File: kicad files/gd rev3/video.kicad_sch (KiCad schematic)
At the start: 55 parts, among them J17 VGA_Micro, J18 vga_SWD, J22 L77HDE15SD1CH4F, SW6 VGA Boot Sel, SW7 VGA RESET, U19 W25Q128JVS, U22 74HCT245, U23 RP2040, U24 74LVC2G04, U25 74LVC2G04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

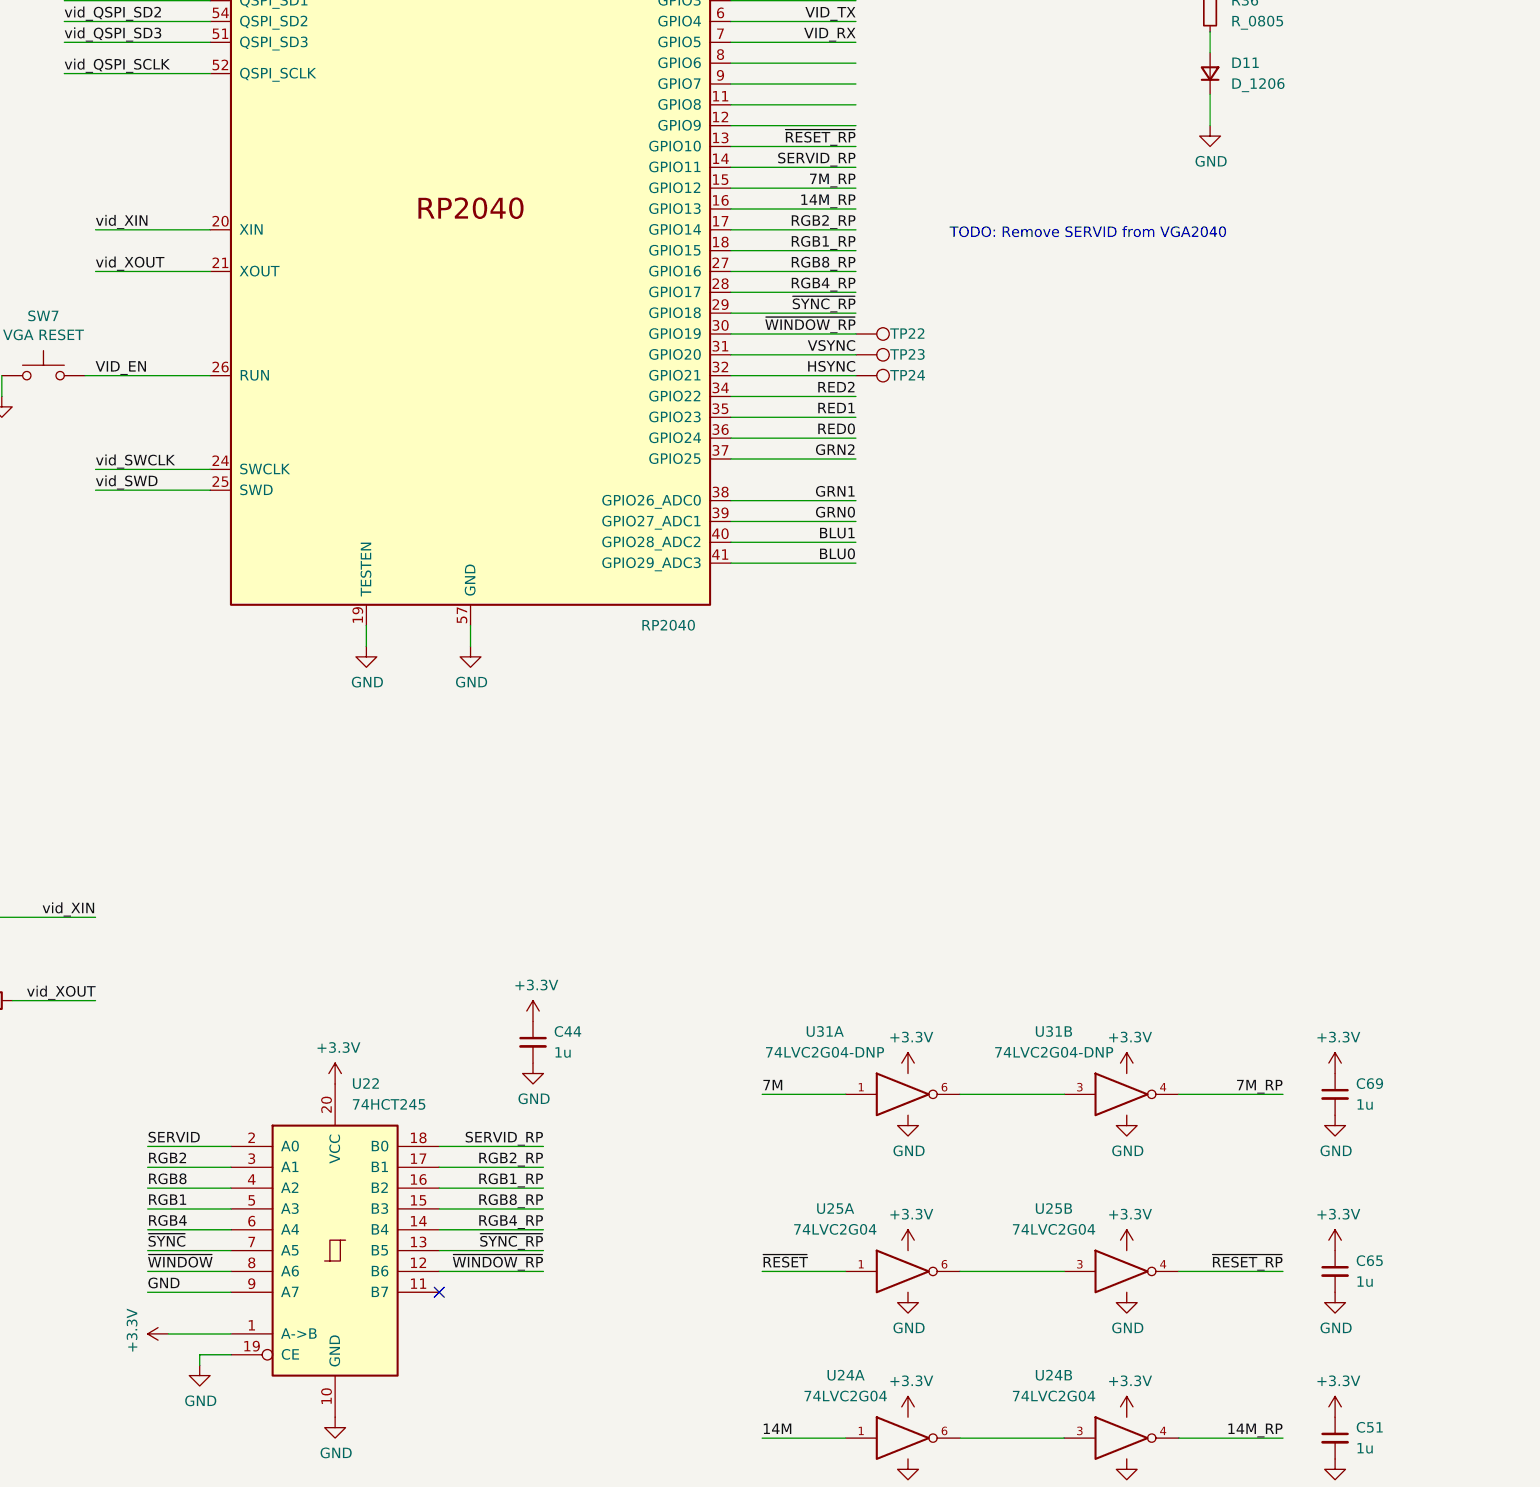
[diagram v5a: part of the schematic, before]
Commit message: started vga and gameport rough route - may remove vga-usb and move earphone to front
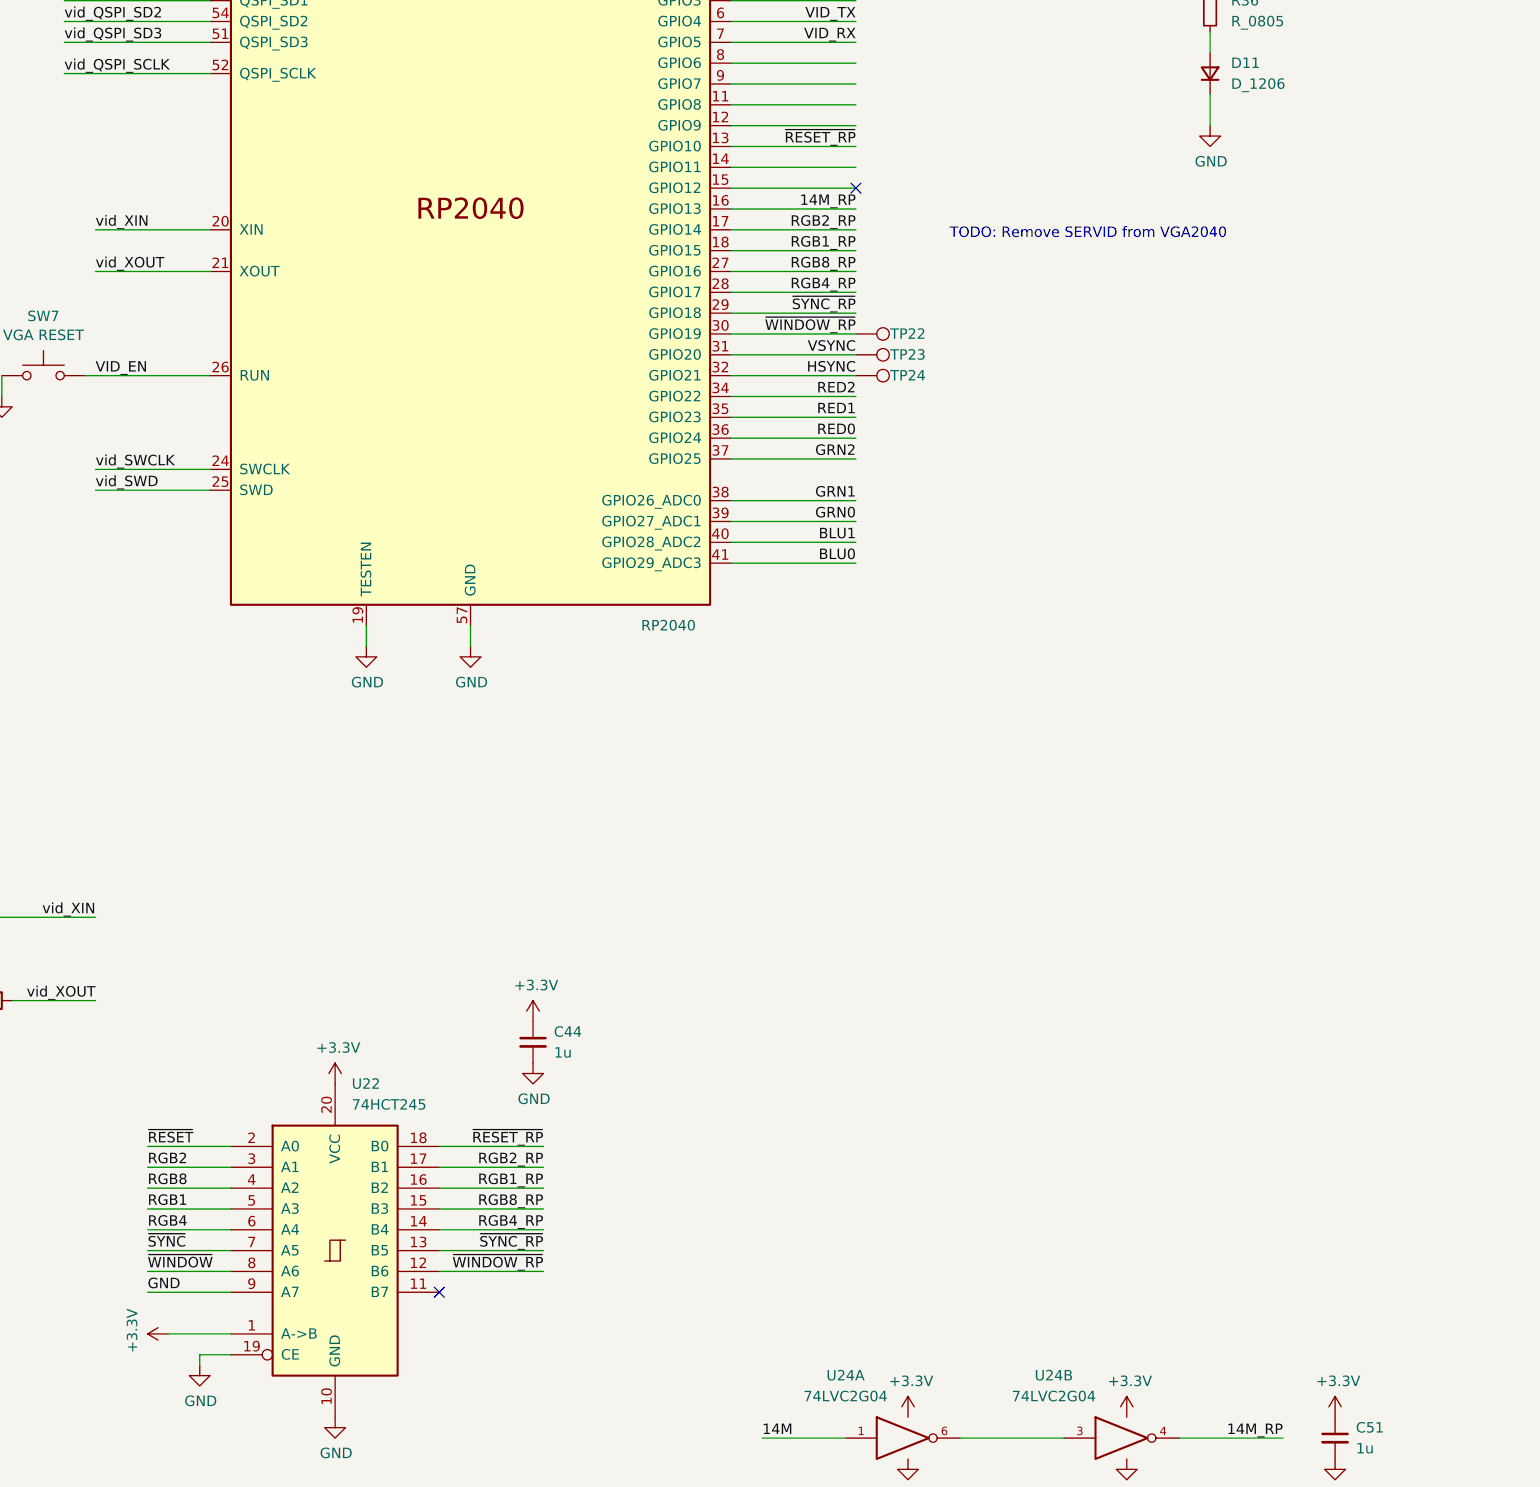
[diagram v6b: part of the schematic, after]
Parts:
- removed C65, C69: 1u, Capacitor_SMD:C_0805_2012Metric, symbol My Library:C_0805
- removed U25: 74LVC2G04, Package_TO_SOT_SMD:SOT-23-6, symbol 74xGxx:74LVC2G04
- removed U31: 74LVC2G04-DNP, Package_TO_SOT_SMD:SOT-23-6, symbol 74xGxx:74LVC2G04
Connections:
- net SERVID: no longer U22.2 (A0)
- net ~{RESET_RP}: now also U22.18 (B0)
- net ~{RESET}: now also U22.2 (A0)
- net 7M_RP: no longer names the net of U23.15 (GPIO12)
- net SERVID_RP: no longer names the net of U23.14 (GPIO11)
- net SERVID_RP: no longer U22.18 (B0)
- no-connect marks 6 -> 7

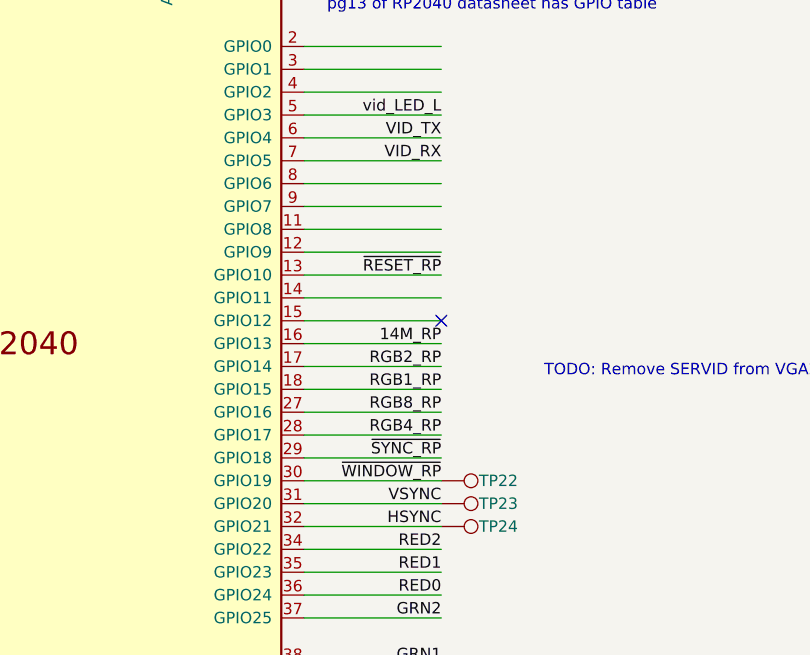
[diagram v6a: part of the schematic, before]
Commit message: aux mem, changed slot, fixed iwm, and RAM addr buses
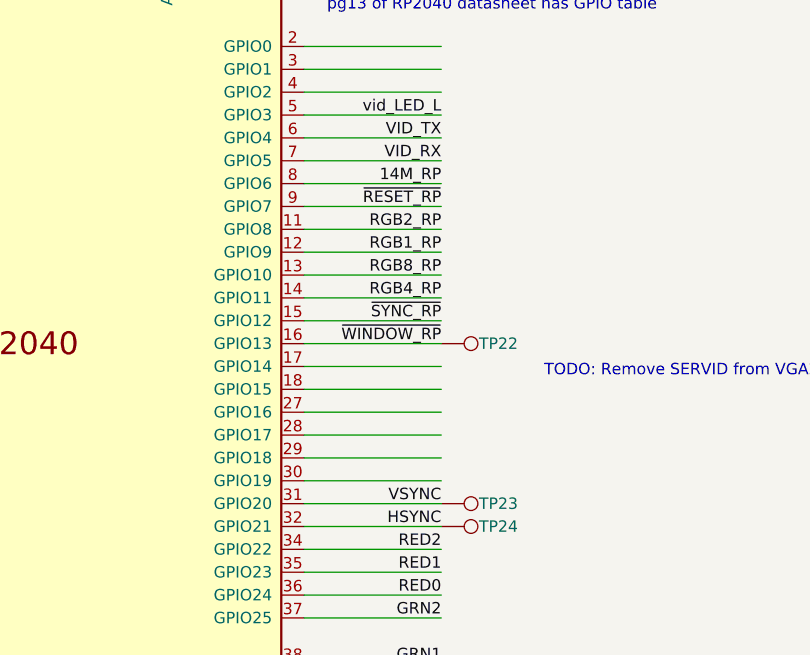
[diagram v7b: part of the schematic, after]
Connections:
- net 14M_RP: now also U23.8 (GPIO6); no longer U23.16 (GPIO13)
- net RGB1_RP: now also U23.12 (GPIO9); no longer U23.18 (GPIO15)
- net RGB2_RP: now also U23.11 (GPIO8); no longer U23.17 (GPIO14)
- net RGB4_RP: now also U23.14 (GPIO11); no longer U23.28 (GPIO17)
- net RGB8_RP: now also U23.13 (GPIO10); no longer U23.27 (GPIO16)
- net ~{RESET_RP}: now also U23.9 (GPIO7); no longer U23.13 (GPIO10)
- net ~{SYNC_RP}: now also U23.15 (GPIO12); no longer U23.29 (GPIO18)
- net ~{WINDOW_RP}: now also U23.16 (GPIO13); no longer U23.30 (GPIO19)
- no-connect marks 7 -> 6
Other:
- moved on the sheet: TP22
